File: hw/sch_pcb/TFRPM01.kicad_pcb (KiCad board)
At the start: 2 copper layers, 37.5 x 19 mm, 28 parts, among them J1 HEADER_1x03, J2 SM04B-GHS-TB, J3 SM04B-GHS-TB, M2 M3, U1 PCF8583, U2 SN74LVC1G14-Q1, U3 MIC5504-3.3YM5

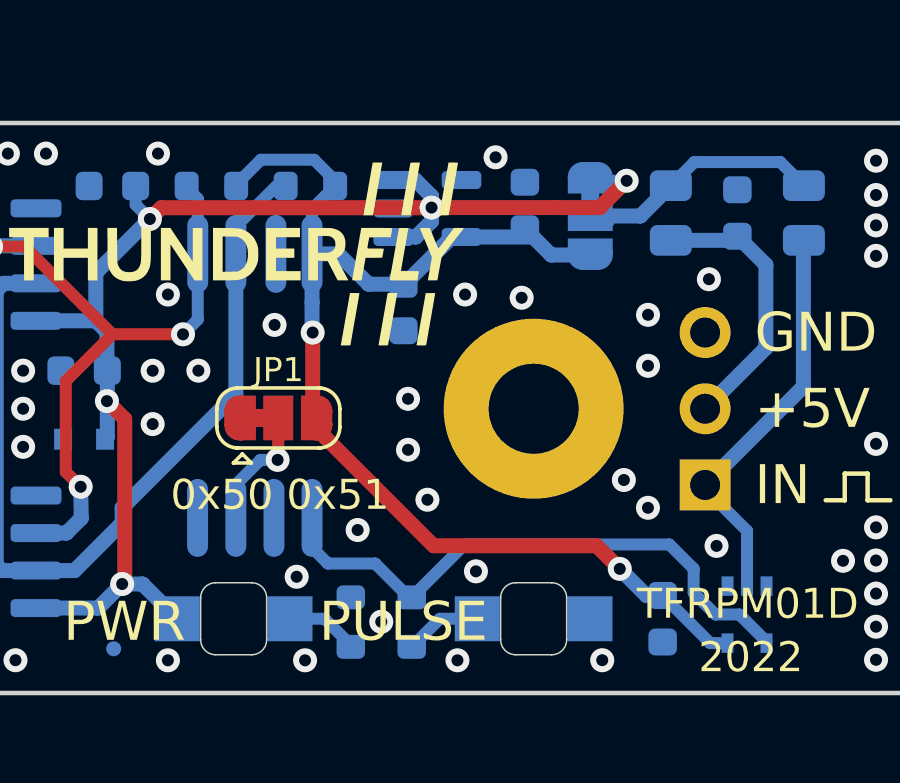
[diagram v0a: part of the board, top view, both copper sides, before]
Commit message: Upgrade PCB from schematics. Minor layout improvement of sharp track in case of LED and U2 pads.
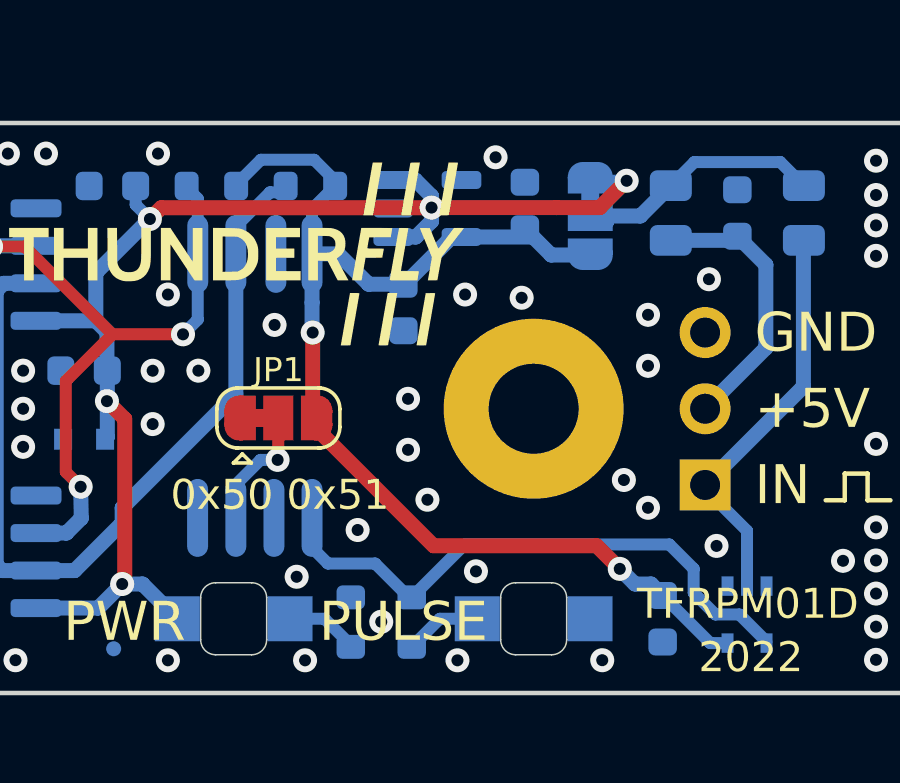
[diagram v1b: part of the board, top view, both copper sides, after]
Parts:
- J1: value HEADER_1x03 -> HEADER_1x03_Horizontal
- U1: value PCF8583 -> PCF8583T
- U2: value SN74LVC1G14-Q1 -> SN74LVC1G14QDCKRQ1
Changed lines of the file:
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@@
   (paper "A4")
   (title_block
-    (date "2022-03-05_07-52-51")
+    (title "TFRPM01D")
+    (date "2023-05-26")
     (company "ThunderFly s.r.o.")
+    (comment 1 "RPM measuring device for UAVs")
+    (comment 2 "Jacho  <info@thunderfly.cz>")
+    (comment 3 "roman-dvorak")
+    (comment 4 "kaklik")
   )
   (layers
@@
     (property "Sheetfile" "TFRPM01.kicad_sch")
     (property "Sheetname" "")
-    (attr exclude_from_pos_files)
+    (property "exclude_from_bom" "")
+    (attr exclude_from_pos_files exclude_from_bom)
     (fp_text reference "JP1" (at 0 -1.6002) (layer "F.SilkS")
       (effects (font (size 0.8 0.8) (thickness 0.1)))
@@
     (property "Sheetfile" "TFRPM01.kicad_sch")
     (property "Sheetname" "")
-    (attr through_hole exclude_from_pos_files)
+    (property "exclude_from_bom" "")
+    (attr through_hole exclude_from_pos_files exclude_from_bom)
     (fp_text reference "M2" (at 0 4.191) (layer "B.SilkS") hide
       (effects (font (size 1.524 1.524) (thickness 0.3048)) (justify mirror))
@@
       (effects (font (size 0.8 0.8) (thickness 0.1)) (justify mirror))
     )
-    (fp_text value "HEADER_1x03" (at 4.385 -7.35) (layer "B.Fab") hide
+    (fp_text value "HEADER_1x03_Horizontal" (at 4.385 -7.35) (layer "B.Fab") hide
       (effects (font (size 1 1) (thickness 0.15)) (justify mirror))
     )
@@
       (effects (font (size 0.9 0.9) (thickness 0.1)) (justify mirror))
     )
-    (fp_text value "PCF8583" (at 0 0) (layer "B.SilkS") hide
+    (fp_text value "PCF8583T" (at 0 0) (layer "B.SilkS") hide
       (effects (font (size 1.524 1.524) (thickness 0.3048)) (justify mirror))
     )
@@
     (property "Sheetfile" "TFRPM01.kicad_sch")
     (property "Sheetname" "")
-    (attr smd)
+    (property "exclude_from_bom" "")
+    (attr smd exclude_from_bom)
     (fp_text reference "FID3" (at 0 1.7145 90) (layer "B.SilkS") hide
       (effects (font (size 1 1) (thickness 0.15)) (justify mirror))
@@
       (effects (font (size 0.8 0.8) (thickness 0.1)) (justify mirror))
     )
-    (fp_text value "SN74LVC1G14-Q1" (at 0 -2 -90) (layer "B.Fab") hide
+    (fp_text value "SN74LVC1G14QDCKRQ1" (at 0 -2 -90) (layer "B.Fab") hide
       (effects (font (size 1 1) (thickness 0.15)) (justify mirror))
     )
@@
     (property "Sheetfile" "TFRPM01.kicad_sch")
     (property "Sheetname" "")
-    (attr smd)
+    (property "exclude_from_bom" "")
+    (attr smd exclude_from_bom)
     (fp_text reference "FID1" (at 0 1.7145 180) (layer "B.SilkS") hide
       (effects (font (size 1 1) (thickness 0.15)) (justify mirror))
@@
     (property "Sheetfile" "TFRPM01.kicad_sch")
     (property "Sheetname" "")
-    (attr smd)
+    (property "exclude_from_bom" "")
+    (attr smd exclude_from_bom)
     (fp_text reference "FID2" (at 0 1.7145 180) (layer "B.SilkS") hide
       (effects (font (size 1 1) (thickness 0.15)) (justify mirror))
@@
     (property "Sheetfile" "TFRPM01.kicad_sch")
     (property "Sheetname" "")
-    (attr exclude_from_pos_files)
+    (property "exclude_from_bom" "")
+    (attr exclude_from_pos_files exclude_from_bom)
     (fp_text reference "JP2" (at 2.8212 -0.1953) (layer "B.SilkS")
       (effects (font (size 0.8 0.8) (thickness 0.1)) (justify mirror))
@@
   (via (at 135.4582 137.668) (size 0.8) (drill 0.4) (layers "F.Cu" "B.Cu") (net 4))
   (segment (start 125.201 127.956) (end 125.201 125.676) (width 0.4) (layer "B.Cu") (net 4))
+  (segment (start 136.888 138.556096) (end 136.505 138.173096) (width 0.5) (layer "B.Cu") (net 4))
   (segment (start 125.201 129.770096) (end 125.201 128.796096) (width 0.5) (layer "B.Cu") (net 4))
   (segment (start 125.201 128.796096) (end 125.201 127.169096) (width 0.5) (layer "B.Cu") (net 4))
   (segment (start 139.05 140.142) (end 138.473904 140.142) (width 0.4) (layer "B.Cu") (net 4))
   (segment (start 128.283 128.1808) (end 129.8578 126.606) (width 0.5) (layer "B.Cu") (net 4))
-  (segment (start 136.346296 138.556096) (end 135.4582 137.668) (width 0.5) (layer "B.Cu") (net 4))
+  (segment (start 135.963296 138.173096) (end 135.4582 137.668) (width 0.5) (layer "B.Cu") (net 4))
   (segment (start 127.0886 128.1808) (end 128.2446 128.1808) (width 0.5) (layer "B.Cu") (net 4))
   (segment (start 125.971 124.731) (end 125.27148 124.03148) (width 0.4) (layer "B.Cu") (net 4))
+  (segment (start 136.505 138.173096) (end 135.963296 138.173096) (width 0.5) (layer "B.Cu") (net 4))
   (segment (start 129.8578 126.606) (end 130.1835 126.606) (width 0.5) (layer "B.Cu") (net 4))
   (segment (start 134.546 127.206) (end 133.171 127.206) (width 0.5) (layer "B.Cu") (net 4))
@@
   (segment (start 123.49552 124.03148) (end 122.621 124.906) (width 0.4) (layer "B.Cu") (net 4))
   (segment (start 138.473904 140.142) (end 136.888 138.556096) (width 0.4) (layer "B.Cu") (net 4))
-  (segment (start 136.888 138.556096) (end 136.346296 138.556096) (width 0.5) (layer "B.Cu") (net 4))
   (segment (start 133.171 127.206) (end 132.296 126.331) (width 0.5) (layer "B.Cu") (net 4))
   (segment (start 120.170904 125.631096) (end 129.1788 125.631096) (width 0.5) (layer "F.Cu") (net 5))
@@
   (segment (start 114.675 137.532096) (end 114.675 128.400096) (width 0.5) (layer "B.Cu") (net 7))
   (segment (start 116 137.725) (end 114.867904 137.725) (width 0.5) (layer "B.Cu") (net 7))
-  (segment (start 124.011096 124.906) (end 122.661 126.256096) (width 0.4) (layer "B.Cu") (net 7))
+  (segment (start 124.321 124.906) (end 124.109504 125.117496) (width 0.4) (layer "B.Cu") (net 7))
   (segment (start 114.675 128.400096) (end 114.925096 128.15) (width 0.5) (layer "B.Cu") (net 7))
+  (segment (start 123.7996 125.117496) (end 122.661 126.256096) (width 0.4) (layer "B.Cu") (net 7))
   (segment (start 118.872 135.633096) (end 118.872 136.141096) (width 0.5) (layer "B.Cu") (net 7))
   (segment (start 122.661 131.844096) (end 118.872 135.633096) (width 0.5) (layer "B.Cu") (net 7))
@@
   (segment (start 118.872 136.141096) (end 117.288096 137.725) (width 0.5) (layer "B.Cu") (net 7))
   (segment (start 122.661 127.956) (end 122.661 131.844096) (width 0.5) (layer "B.Cu") (net 7))
+  (segment (start 124.109504 125.117496) (end 123.7996 125.117496) (width 0.4) (layer "B.Cu") (net 7))
   (segment (start 128.432696 138.618096) (end 127.3048 137.4902) (width 0.4) (layer "B.Cu") (net 8))
   (segment (start 139.446 139.189096) (end 140.35 140.093096) (width 0.4) (layer "B.Cu") (net 8))

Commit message: Upgrade PCB from schematics.
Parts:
- J1: value HEADER_1x03_Horizontal -> DS1022-1*40RDF11-B
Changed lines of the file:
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@@
       (effects (font (size 0.8 0.8) (thickness 0.1)) (justify mirror))
     )
-    (fp_text value "HEADER_1x03_Horizontal" (at 4.385 -7.35) (layer "B.Fab") hide
+    (fp_text value "DS1022-1*40RDF11-B" (at 4.385 -7.35) (layer "B.Fab") hide
       (effects (font (size 1 1) (thickness 0.15)) (justify mirror))
     )

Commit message: Update LEDs part numbers.
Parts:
- D2: value LED RED -> KPTR-3216SURCK
- D3: value LED GREEN -> KPTR-3216CGCK
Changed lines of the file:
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@@
     (descr "Diode Mini-MELF Standard")
     (tags "Diode Mini-MELF Standard")
+    (property "Color" "Red")
     (property "Sheetfile" "TFRPM01.kicad_sch")
     (property "Sheetname" "")
-    (property "UST_ID" "5c70984412875079b91f8896")
     (attr smd)
     (fp_text reference "D2" (at 1.8034 -1.790096 180) (layer "B.SilkS")
       (effects (font (size 0.8 0.8) (thickness 0.1)) (justify mirror))
     )
-    (fp_text value "LED RED" (at 0 -3.81 180) (layer "B.SilkS") hide
+    (fp_text value "KPTR-3216SURCK" (at 0 -3.81 180) (layer "B.SilkS") hide
       (effects (font (size 1.524 1.524) (thickness 0.3048)) (justify mirror))
     )
@@
     (descr "Diode Mini-MELF Standard")
     (tags "Diode Mini-MELF Standard")
+    (property "Color" "Green")
     (property "Sheetfile" "TFRPM01.kicad_sch")
     (property "Sheetname" "")
-    (property "UST_ID" "5c70984412875079b91f8895")
-    (property "UST_id" "")
     (attr smd)
     (fp_text reference "D3" (at -2.573 -1.637696 180) (layer "B.SilkS")
       (effects (font (size 0.8 0.8) (thickness 0.1)) (justify mirror))
     )
-    (fp_text value "LED GREEN" (at 0 -3.81 180) (layer "B.SilkS") hide
+    (fp_text value "KPTR-3216CGCK" (at 0 -3.81 180) (layer "B.SilkS") hide
       (effects (font (size 1.524 1.524) (thickness 0.3048)) (justify mirror))
     )

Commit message: Updated year mark in silkscreen.
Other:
- board text added: "2023"
- board text removed: "2022"
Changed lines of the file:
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@@
     (effects (font (size 1.3 1.3) (thickness 0.15)) (justify left))
   )
-  (gr_text "2022" (at 139.827 140.6144) (layer "F.SilkS")
+  (gr_text "2023" (at 139.827 140.6144) (layer "F.SilkS")
     (effects (font (size 1 1) (thickness 0.1)))
   )
